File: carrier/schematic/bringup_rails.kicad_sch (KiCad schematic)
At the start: 26 parts, among them SW401 DSHP04TSGER, SW402 DSHP08TSGER, SW403 TS-1187A-B-A-B, SW404 TS-1187A-B-A-B, SW405 TS-1187A-B-A-B, U401 TCA9535PWR

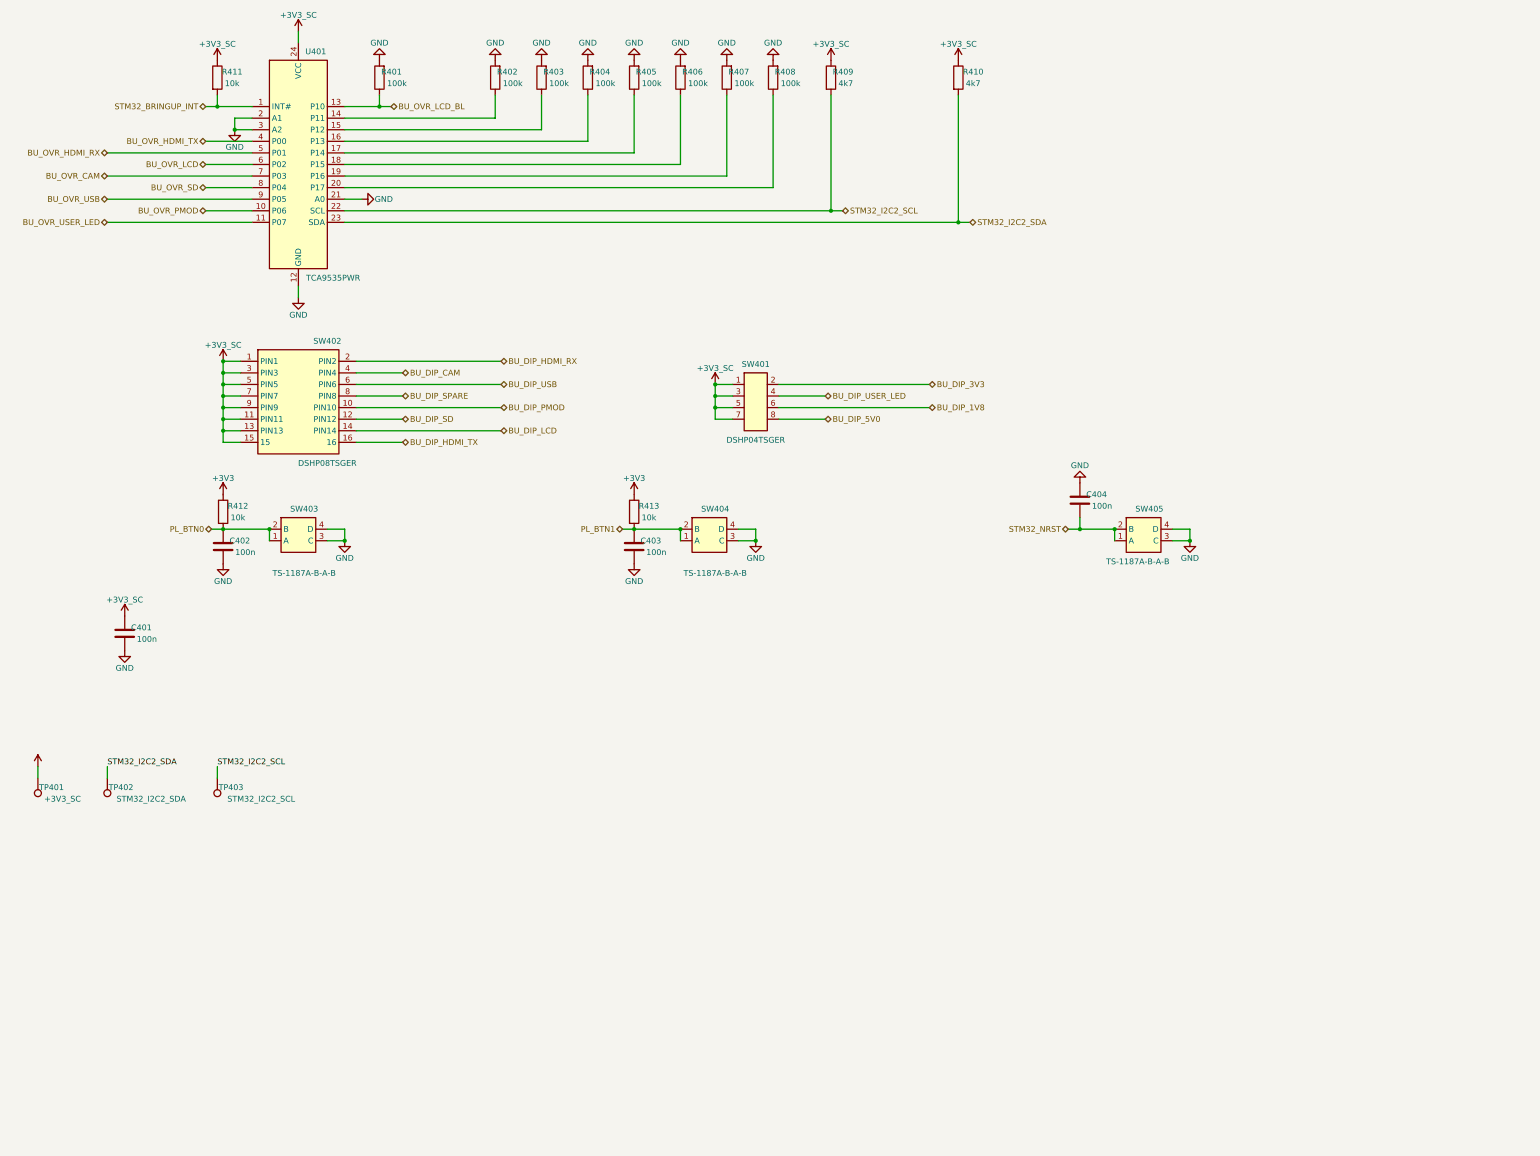
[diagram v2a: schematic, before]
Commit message: bringup: 5V MODULE GATES (PLAN round 5) — +5V_HDMI_TX/+5V_LCD SY6280 cells
Two new module gate cells resolve the power tree's last two UNSOURCED
findings, following the existing per-module pattern exactly:
- bringup_modules U9 +5V -> +5V_HDMI_TX (RSET 13k = 523 mA backstop; the
  load is TPD12S016-internally limited to 55 mA, DS 7.3.10) and U10
  +5V -> +5V_LCD (RSET 6.8k = 1.0 A for the 450 mA boost budget), 100n
  in/out, 1k status LEDs, TPs at the gated source.
- bringup_en_modules: 2 new SN74LVC1G08 AND cells (DIP master, SW veto).
- bringup_rails: SW1/SW2 positions were EXHAUSTED -> honest extension DIP
  SW6 (DSHP04TSGER, already-verified part; pos 1/2 wired, 3/4 author-NC
  spares) + TCA9535 P12/P13 vetos (P11 stays reserved for PMON_ALERT_N).
- bringup_facts.dip_switch_refs(): manual/firmware generators now discover
  every DSHP DIP instead of hard-coding SW1/SW2 — BRINGUP.md + the SC
  contract header regenerated with the new EN map automatically
  (ZC_TCA9535_BIT_EN_HDMI_TX_5V=10 / _EN_LCD_5V=11, SW6 stage-4 rows).
POWER TREE PASS: 14 regulators, findings 4->2, +5V buck at 91 % of 3 A.
All gates green (board exit 0); 3 drifted renders eyeballed full-res and
blessed; PWR_FLAG policy auto-stripped the now-driven rails' flags.

Co-Authored-By: Claude Fable 5 <noreply@anthropic.com>
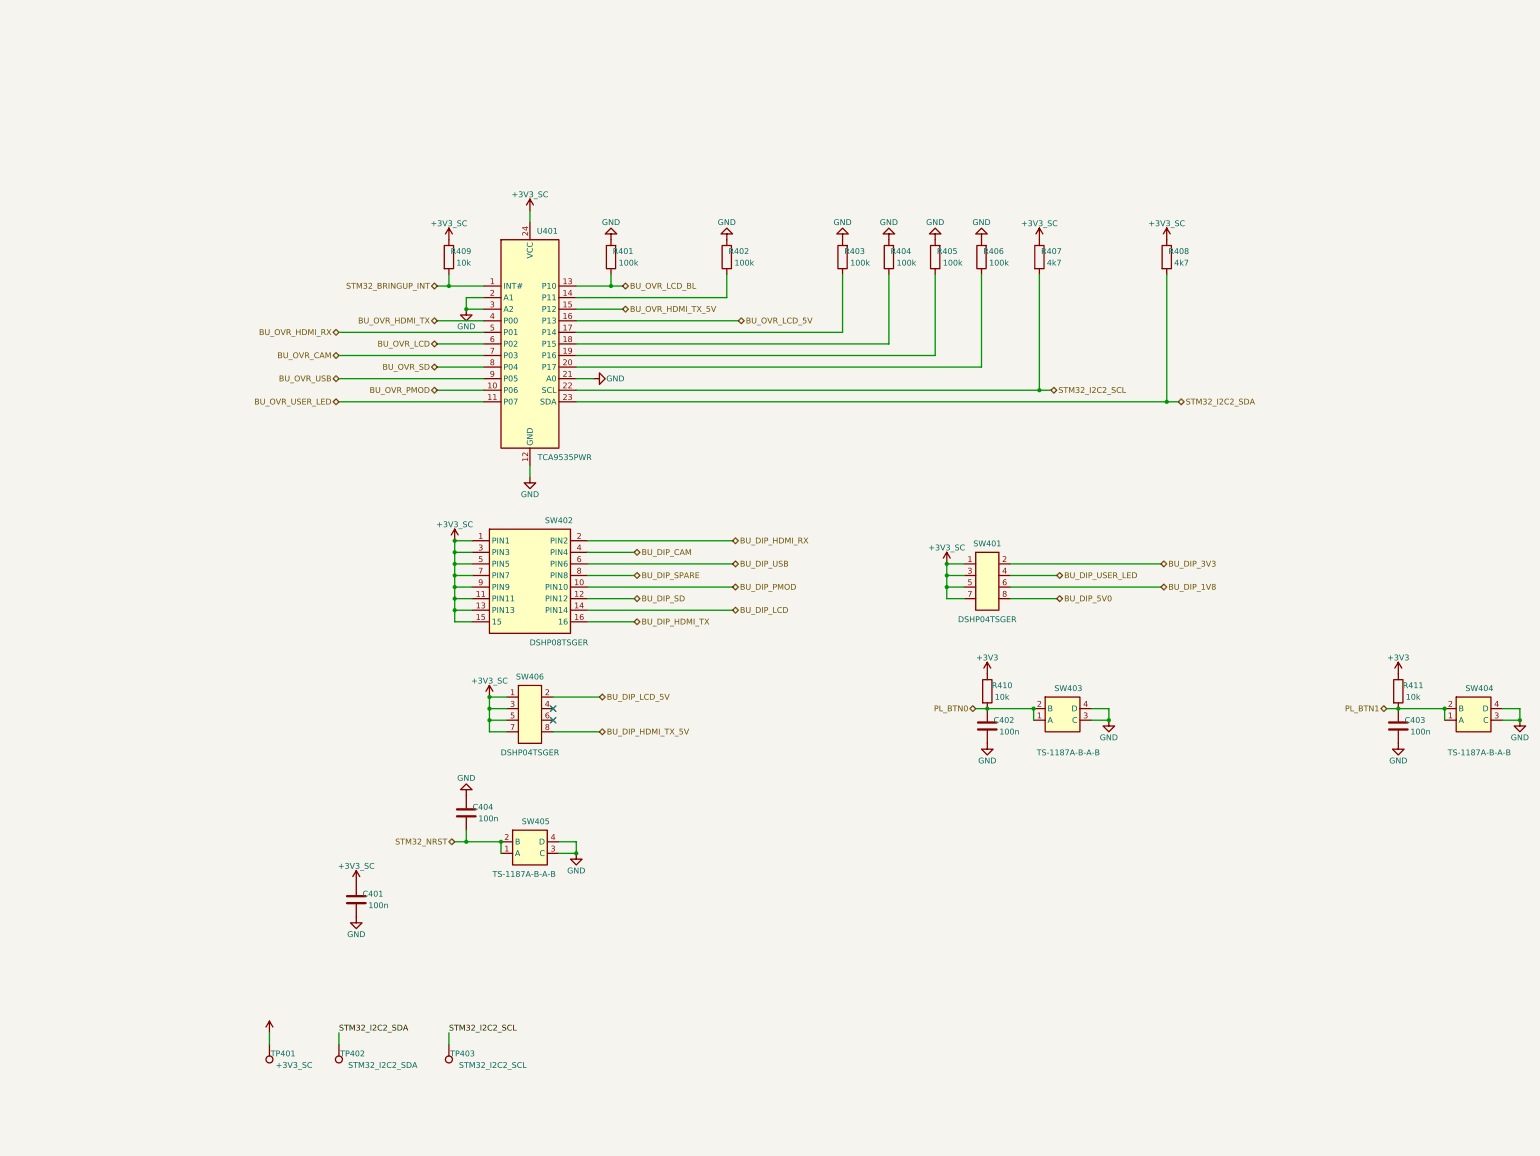
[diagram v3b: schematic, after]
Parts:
- removed TP403: STM32_I2C2_SCL, TestPoint:TestPoint_Pad_D1.5mm, symbol Connector:TestPoint
- C402: renamed from R412; value 10k -> 100n; footprint Resistor_SMD:R_0603_1608Metric -> Capacitor_SMD:C_0603_1608Metric; symbol Device:R -> Device:C; LCSC C25804 -> C1591
- C403: renamed from R413; value 10k -> 100n; footprint Resistor_SMD:R_0603_1608Metric -> Capacitor_SMD:C_0603_1608Metric; symbol Device:R -> Device:C; LCSC C25804 -> C1591
- C404: renamed from SW405; value TS-1187A-B-A-B -> 100n; footprint TS-1187A-B-A-B:TS-1187A-B-A-B -> Capacitor_SMD:C_0603_1608Metric; symbol TS-1187A-B-A-B:TS-1187A-B-A-B -> Device:C; LCSC C318884 -> C1591
- R407, R408: value 100k -> 4k7; LCSC C25803 -> C23162
- R410: renamed from SW403; value TS-1187A-B-A-B -> 10k; footprint TS-1187A-B-A-B:TS-1187A-B-A-B -> Resistor_SMD:R_0603_1608Metric; symbol TS-1187A-B-A-B:TS-1187A-B-A-B -> Device:R; LCSC C318884 -> C25804
- R411: renamed from SW404; value TS-1187A-B-A-B -> 10k; footprint TS-1187A-B-A-B:TS-1187A-B-A-B -> Resistor_SMD:R_0603_1608Metric; symbol TS-1187A-B-A-B:TS-1187A-B-A-B -> Device:R; LCSC C318884 -> C25804
- SW401: renamed from R410; value 4k7 -> DSHP04TSGER; footprint Resistor_SMD:R_0603_1608Metric -> DSHP04TSGER:DSHP04TSGER; symbol Device:R -> DSHP04TSGER:DSHP04TSGER; LCSC C23162 -> C3293144
- SW402: renamed from R409; value 4k7 -> DSHP08TSGER; footprint Resistor_SMD:R_0603_1608Metric -> DSHP08TSGER:DSHP08TSGER; symbol Device:R -> DSHP08TSGER:DSHP08TSGER; LCSC C23162 -> C3293147
- SW403: renamed from SW401; value DSHP04TSGER -> TS-1187A-B-A-B; footprint DSHP04TSGER:DSHP04TSGER -> TS-1187A-B-A-B:TS-1187A-B-A-B; symbol DSHP04TSGER:DSHP04TSGER -> TS-1187A-B-A-B:TS-1187A-B-A-B; LCSC C3293144 -> C318884
- SW404: renamed from C402; value 100n -> TS-1187A-B-A-B; footprint Capacitor_SMD:C_0603_1608Metric -> TS-1187A-B-A-B:TS-1187A-B-A-B; symbol Device:C -> TS-1187A-B-A-B:TS-1187A-B-A-B; LCSC C1591 -> C318884
- SW405: renamed from C403; value 100n -> TS-1187A-B-A-B; footprint Capacitor_SMD:C_0603_1608Metric -> TS-1187A-B-A-B:TS-1187A-B-A-B; symbol Device:C -> TS-1187A-B-A-B:TS-1187A-B-A-B; LCSC C1591 -> C318884
- SW406: renamed from SW402; value DSHP08TSGER -> DSHP04TSGER; footprint DSHP08TSGER:DSHP08TSGER -> DSHP04TSGER:DSHP04TSGER; symbol DSHP08TSGER:DSHP08TSGER -> DSHP04TSGER:DSHP04TSGER; LCSC C3293147 -> C3293144
- TP401: renamed from C401; value 100n -> +3V3_SC; footprint Capacitor_SMD:C_0603_1608Metric -> TestPoint:TestPoint_Pad_D1.5mm; symbol Device:C -> Connector:TestPoint; BOM (none) -> exclude; LCSC C1591 -> (none)
- TP402: renamed from TP401; value +3V3_SC -> STM32_I2C2_SDA
- TP403: renamed from TP402; value STM32_I2C2_SDA -> STM32_I2C2_SCL
- renumbered C404 to C401, R411 to R409
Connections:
- net +3V3: now also R410.1, R411.1; no longer C402.1, C403.1
- net +3V3_SC: now also C401.1, R407.1, R408.1, SW401.3, SW401.5, SW401.7, SW402.11 (PIN11), SW402.13 (PIN13), SW402.15, SW402.3 (PIN3), SW402.5 (PIN5), SW402.7 (PIN7), SW402.9 (PIN9); no longer SW403.1, SW403.3, SW403.5, SW403.7, SW406.11 (PIN11), SW406.13 (PIN13), SW406.15, SW406.9 (PIN9), TP402.1
- net BU_DIP_1V8: now also SW401.6; no longer SW403.6
- net BU_DIP_3V3: now also SW401.2; no longer SW403.2
- net BU_DIP_5V0: now also SW401.8; no longer SW403.8
- net BU_DIP_CAM: now also SW402.4 (PIN4); no longer SW406.4 (PIN4)
- net BU_DIP_HDMI_RX: now also SW402.2 (PIN2); no longer SW406.2 (PIN2)
- net BU_DIP_HDMI_TX: now also SW402.16; no longer SW406.16
- net BU_DIP_LCD: now also SW402.14 (PIN14); no longer SW406.14 (PIN14)
- net BU_DIP_PMOD: now also SW402.10 (PIN10); no longer SW406.10 (PIN10)
- net BU_DIP_SD: now also SW402.12 (PIN12); no longer SW406.12 (PIN12)
- net BU_DIP_SPARE: now also SW402.8 (PIN8); no longer SW406.8 (PIN8)
- net BU_DIP_USB: now also SW402.6 (PIN6); no longer SW406.6 (PIN6)
- net BU_DIP_USER_LED: now also SW401.4; no longer SW403.4
- net GND: now also C402.2, C403.2, C404.2, SW403.3 (C), SW403.4 (D), SW404.3 (C), SW404.4 (D), SW405.3 (C), SW405.4 (D); no longer C404.3 (C), C404.4 (D), R407.2, R408.2, R410.3 (C), R410.4 (D), R411.3 (C), R411.4 (D), SW404.2, SW405.2, TP401.2
- net PL_BTN0: now also C402.1, SW403.1 (A), SW403.2 (B); no longer C402.2, R410.1 (A), SW404.1
- net PL_BTN1: now also C403.1, SW404.1 (A), SW404.2 (B); no longer C403.2, R411.1 (A), SW405.1
- net STM32_I2C2_SCL: now also R407.2, TP403.1; no longer SW402.2
- net STM32_I2C2_SDA: now also R408.2, TP402.1; no longer SW401.2, TP403.1
- net STM32_NRST: now also SW405.1 (A), SW405.2 (B); no longer C401.1, C404.2 (B)
- net at R404.1: now also U401.18 (P15); no longer U401.16 (P13)
- net at R403.1: now also U401.17 (P14); no longer U401.15 (P12)
- net at R406.1: now also U401.20 (P17); no longer U401.18 (P15)
- net at U401.19 (P16): now also R405.1; no longer R407.1
- new net BU_DIP_HDMI_TX_5V: SW406.8
- new net BU_DIP_LCD_5V: SW406.2
- new net BU_OVR_HDMI_TX_5V: U401.15 (P12)
- new net BU_OVR_LCD_5V: U401.16 (P13)
- no-connect marks 0 -> 2
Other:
- moved on the sheet: C401, R401, R402, R403, R404, R405, R406, R407, R408, R409, TP402, TP403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

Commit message: audit-fix(engine): harvest F1-F7,F9 — gate hardening + leak + guards
F1 selftest now exercises the VISUAL gate against geometry mutants (wire-cross
+ text-over-wire) — proven to bite (was never run on a mutant before).
F2 visual_gate catches different-net wire T-touch / butt-join shorts.
F3 netlist_gate no longer leaks tmp .net files (was 2671 stale).
F4 board uniquify guards the stride (widened 100->1000) against ref collision.
F5 hier-mode sheets now re-run through the per-sheet netlist gate.
F6 dead clause dropped; F7 stale zynq_eda docstring fixed; F9 eager inline-pin
validation. Source copied verbatim from the audit-fix worktree (6 files, proven
untouched on origin since its base); board regenerated fresh. All gates green,
selftest geo-mutants killed by the visual gate, goldens 23/23, m1_rc PASS.

Co-Authored-By: Claude Fable 5 <noreply@anthropic.com>
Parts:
- renumbered C401 to C4001, C402 to C4002, C403 to C4003, C404 to C4004, R401 to R4001, R402 to R4002, R403 to R4003, R404 to R4004, R405 to R4005, R406 to R4006, R407 to R4007, R408 to R4008, R409 to R4009, R410 to R4010, R411 to R4011, SW401 to SW4001, SW402 to SW4002, SW403 to SW4003, SW404 to SW4004, SW405 to SW4005, SW406 to SW4006, TP401 to TP4001, TP402 to TP4002, TP403 to TP4003, U401 to U4001
